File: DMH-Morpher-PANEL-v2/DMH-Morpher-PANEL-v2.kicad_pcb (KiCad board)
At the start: 2 copper layers, 100 x 200 mm, 38 parts, among them J0 Panel_GND_Solder_Wire_Pad

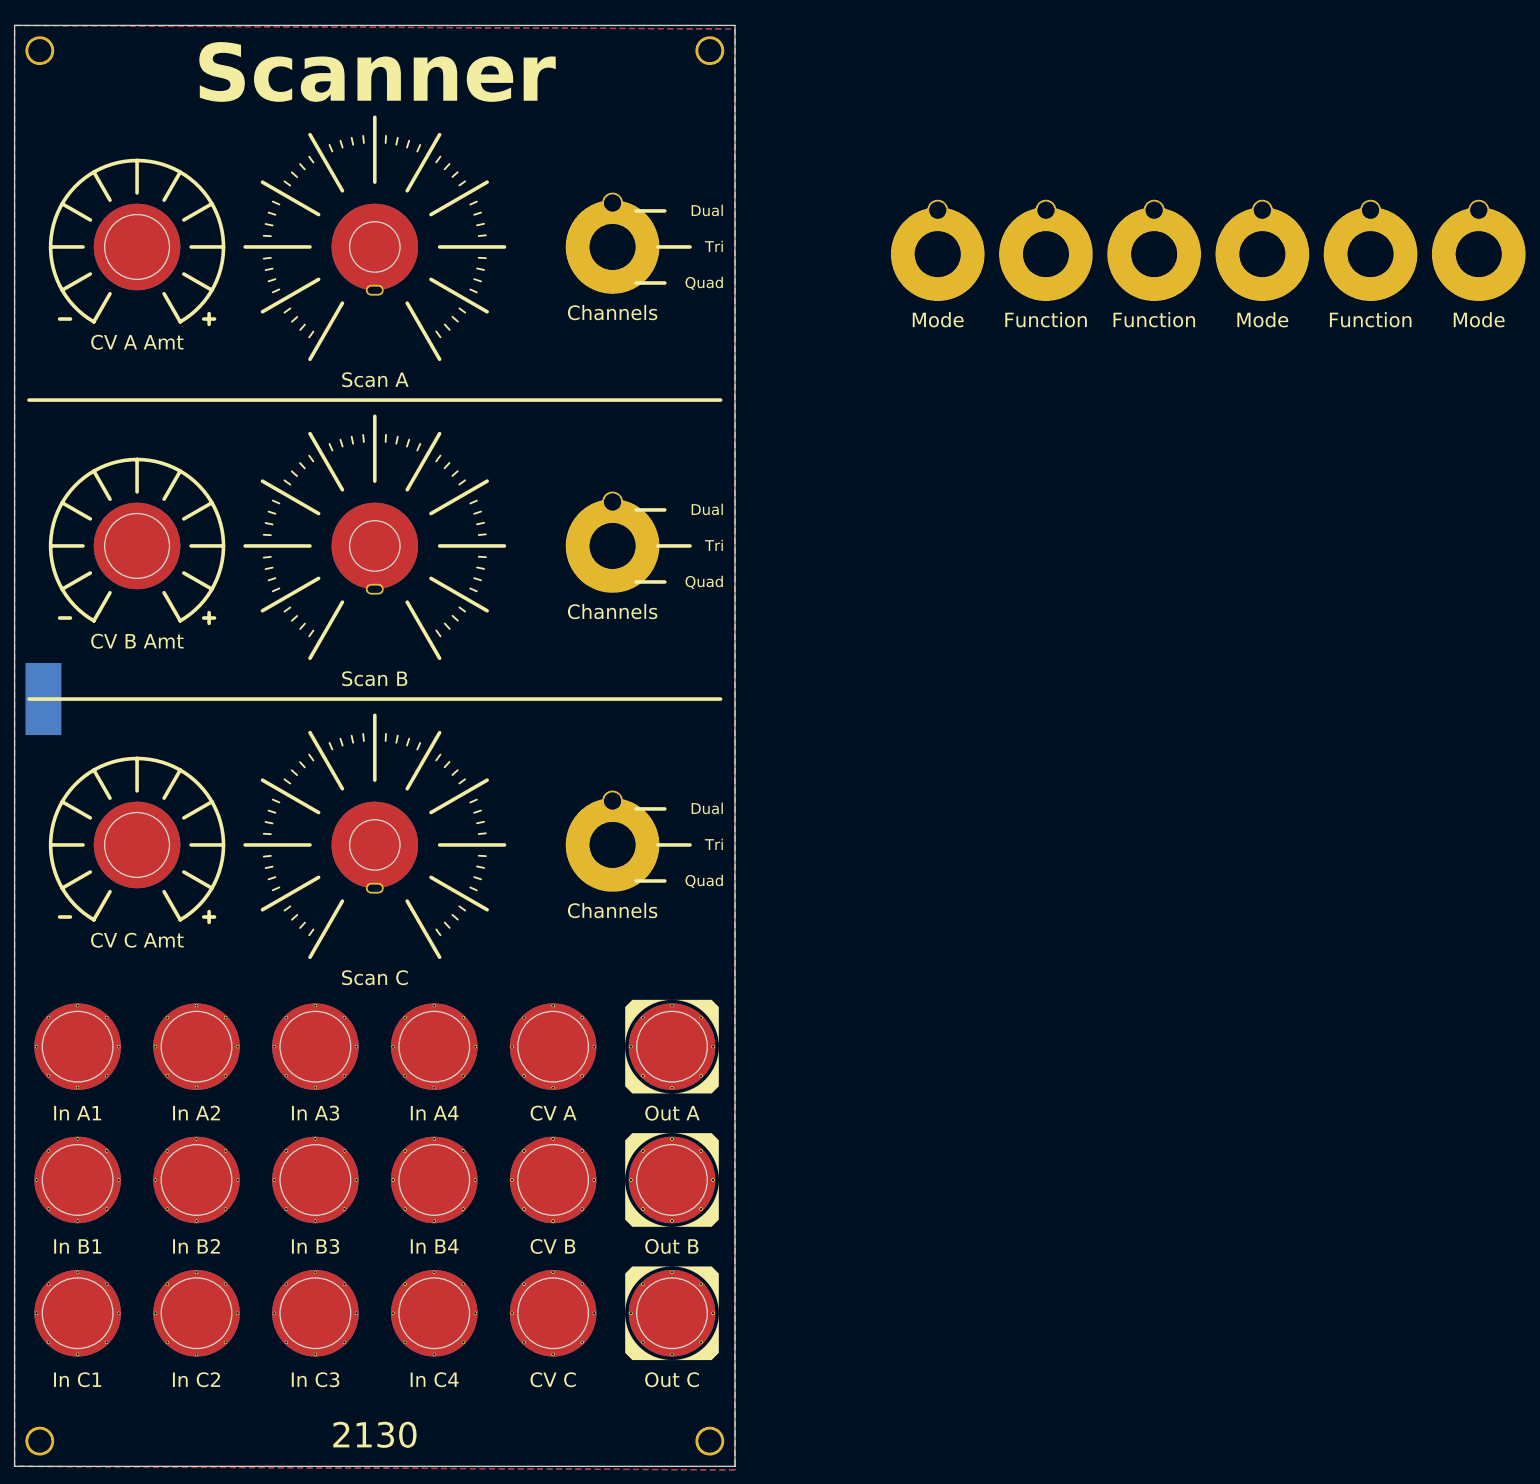
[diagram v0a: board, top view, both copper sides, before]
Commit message: Redesigned panel
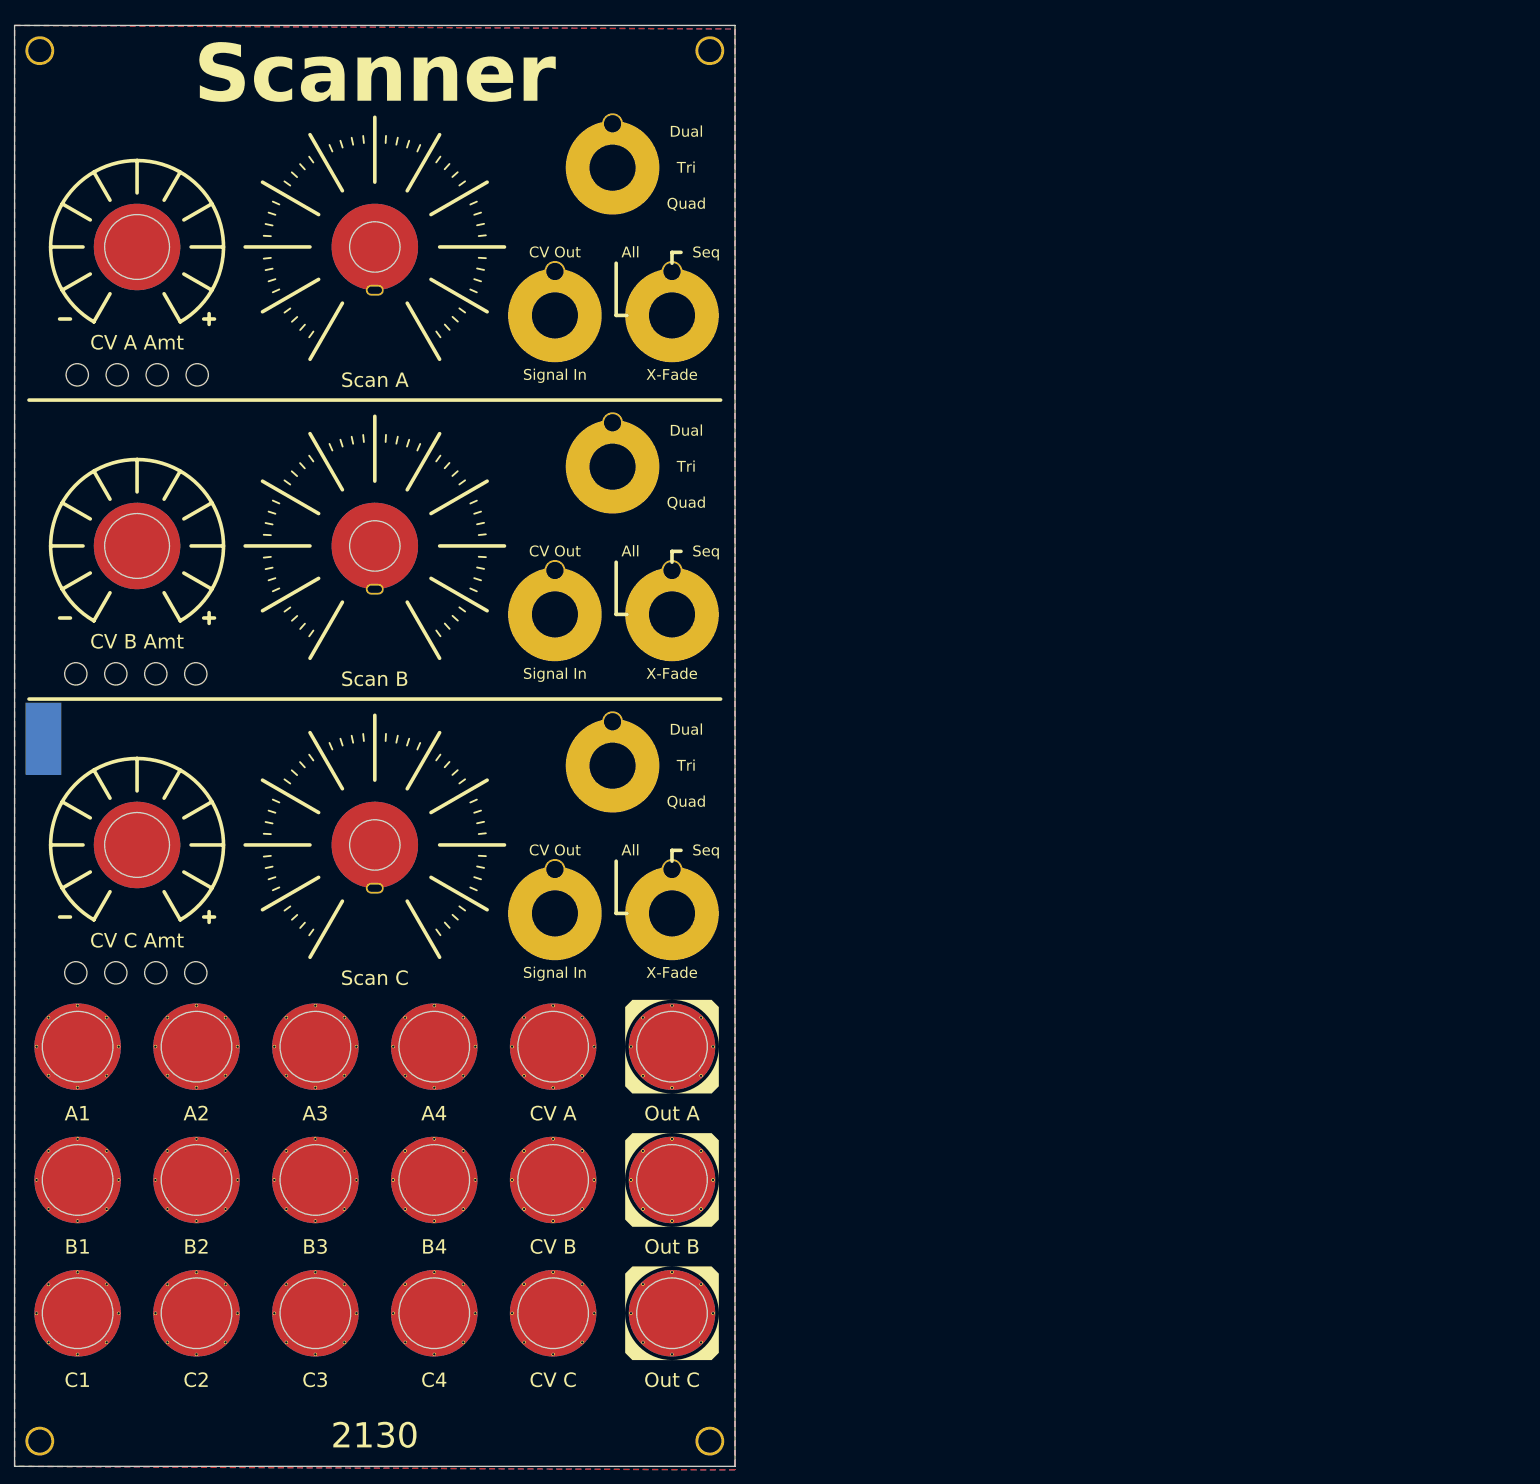
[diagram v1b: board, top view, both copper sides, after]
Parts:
- added H38: LED A1, SynthStuff:MountingHole_LED_3mm_R, F.Cu at (58.7, 78.5)
- added H39: LED A2, SynthStuff:MountingHole_LED_3mm_R, F.Cu at (58.5, 120.0)
- added H40: LED A3, SynthStuff:MountingHole_LED_3mm_R, F.Cu at (58.5, 161.5)
- added H41: LED A4, SynthStuff:MountingHole_LED_3mm_R, F.Cu at (64.2, 78.5)
- added H42: LED B1, SynthStuff:MountingHole_LED_3mm_R, F.Cu at (64.0, 120.0)
- added H43: LED B2, SynthStuff:MountingHole_LED_3mm_R, F.Cu at (64.0, 161.5)
- added H44: LED B3, SynthStuff:MountingHole_LED_3mm_R, F.Cu at (69.8, 78.5)
- added H45: LED B4, SynthStuff:MountingHole_LED_3mm_R, F.Cu at (69.6, 120.0)
- added H46: LED C1, SynthStuff:MountingHole_LED_3mm_R, F.Cu at (69.6, 161.5)
- added H47: LED C2, SynthStuff:MountingHole_LED_3mm_R, F.Cu at (75.3, 78.5)
- added H48: LED C3, SynthStuff:MountingHole_LED_3mm_R, F.Cu at (75.2, 120.0)
- added H49: LED C4, SynthStuff:MountingHole_LED_3mm_R, F.Cu at (75.2, 161.5)
- H11: value In A2 -> A2
- H12: value In B2 -> B2
- H15: value In A3 -> A3
- H17: value In B3 -> B3
- H19: value In A4 -> A4
- H20: value In B4 -> B4
- H21: value In C1 -> C1
- H24: value In C2 -> C2
- H26: value In C3 -> C3
- H28: value In C4 -> C4
- H5: value In A1 -> A1
- H8: value In B1 -> B1
- moved H36 145.6 mm to (125.0, 153.2)
- moved H37 144.6 mm to (141.2, 153.2)
- moved H34 97.0 mm to (125.0, 111.8)
- moved H35 96.0 mm to (141.2, 111.8)
- moved H33 68.7 mm to (125.0, 70.2)
- moved H32 37.9 mm to (141.2, 70.2)
- moved H29 11.0 mm to (133.0, 49.8)
- moved H30 11.0 mm to (133.0, 91.2)
- moved H31 11.0 mm to (133.0, 132.8)
- moved J0 5.50 mm to (54.0, 129.0)
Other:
- board text added: "All"
- board text added: "CV Out"
- board text added: "Seq"
- board text added: "Signal In"
- board text added: "X-Fade"

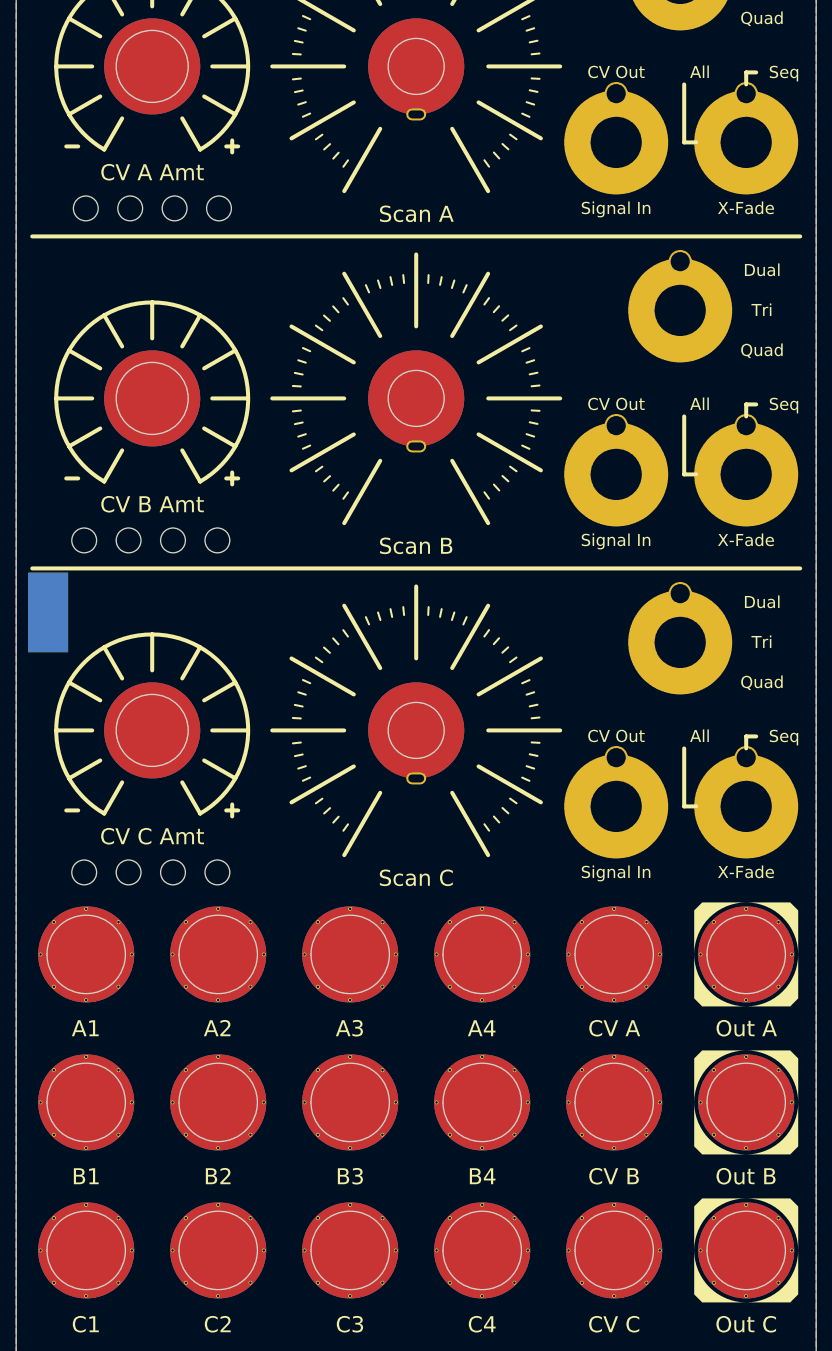
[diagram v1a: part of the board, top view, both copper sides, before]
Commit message: Improved labeling on front panel
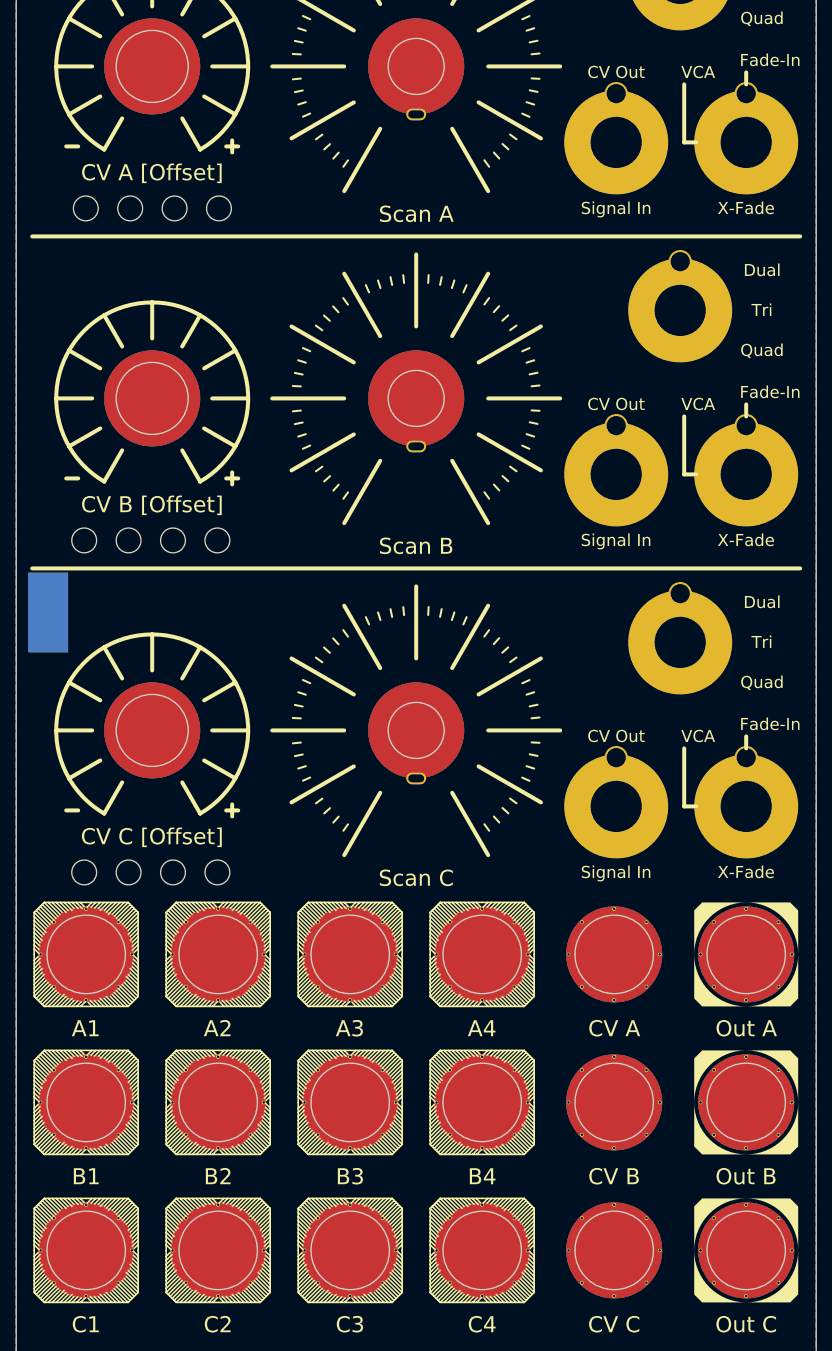
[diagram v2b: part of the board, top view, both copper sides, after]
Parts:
- H11, H12, H15, H17, H19, H20, H21, H24, H26, H28, H5, H8: footprint SynthStuff:Jack_6.35mm_Cutout_v3 -> SynthStuff:Jack_6.35mm_Cutout_IO
- H13: value CV A Amt -> CV A [Offset]
- H14: value CV B Amt -> CV B [Offset]
- H25: value CV C Amt -> CV C [Offset]
- H29, H30, H31: value Channels -> Range
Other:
- board text added: "Fade-In"
- board text added: "VCA"
- board text removed: "All"
- board text removed: "Seq"
